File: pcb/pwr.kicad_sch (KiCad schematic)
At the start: 17 parts, among them IC1 LT8606IDC#TRPBF

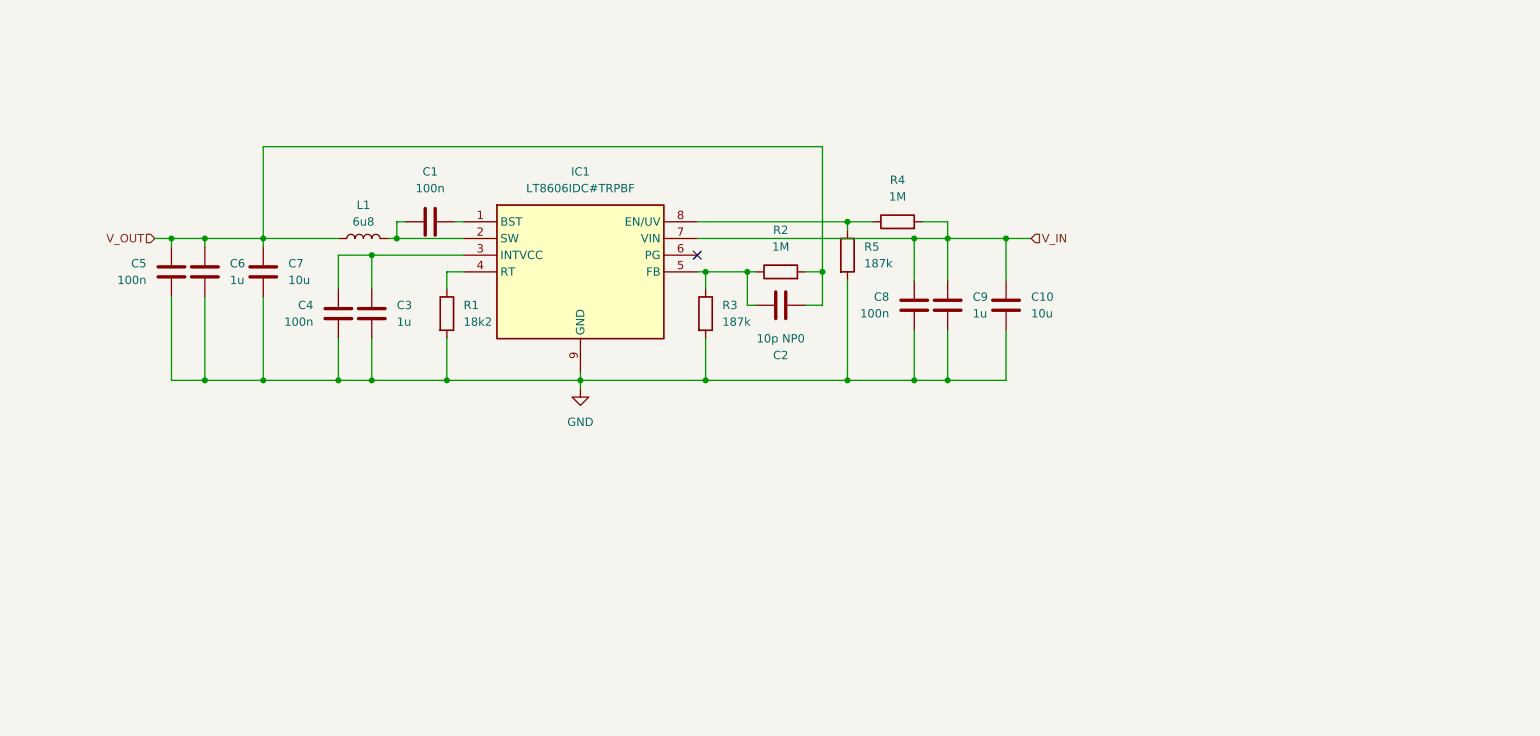
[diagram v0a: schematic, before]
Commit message: Sch almost done, maybe add current sense
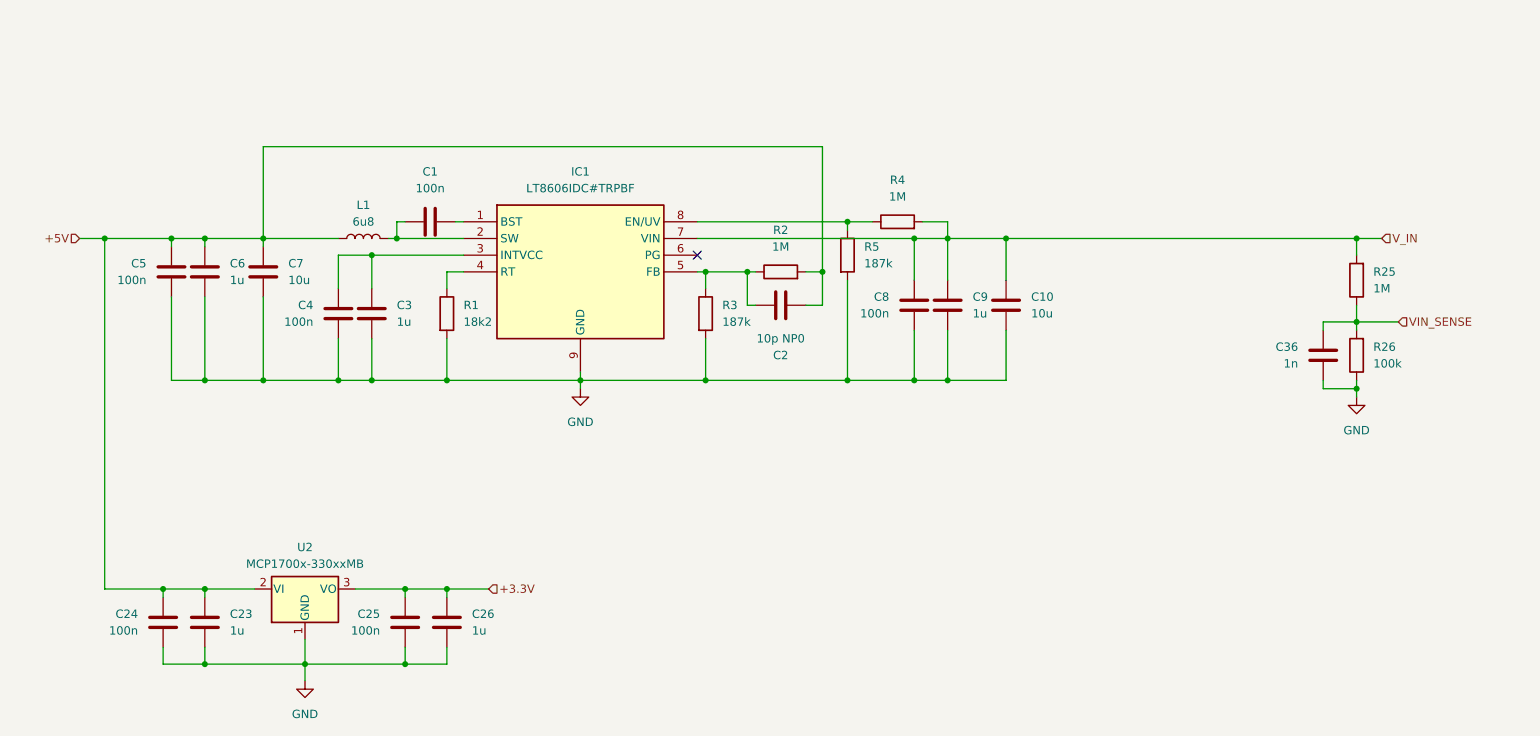
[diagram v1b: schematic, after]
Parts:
- added C23, C26: 1u, Capacitor_SMD:C_0603_1608Metric, symbol Device:C
- added C24, C25: 100n, Capacitor_SMD:C_0603_1608Metric, symbol Device:C
- added C36: 1n, Capacitor_SMD:C_0603_1608Metric, symbol Device:C
- added R25: 1M, Resistor_SMD:R_0603_1608Metric, symbol Device:R
- added R26: 100k, Resistor_SMD:R_0603_1608Metric, symbol Device:R
- added U2: MCP1700x-330xxMB, Package_TO_SOT_SMD:SOT-89-3, symbol Regulator_Linear:MCP1700x-330xxMB
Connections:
- net GND: now also C23.2, C24.1, C25.1, C26.2, C36.1, R26.1, U2.1 (GND)
- net V_IN: now also R25.2
- net V_OUT renamed +5V
- net +5V: now also C23.1, C24.2, U2.2 (VI)
- new net +3.3V: C25.2, C26.1, U2.3 (VO)
- new net VIN_SENSE: C36.2, R25.1, R26.2

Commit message: Scheamtic almost finished, astarted firmware and pcb
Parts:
- added C37: 100n, Capacitor_SMD:C_0603_1608Metric, symbol Device:C
- added D10: BAV199, Package_TO_SOT_SMD:TSOT-23, symbol Device:D_Dual_Series_AKC
- added R27: 500m, Resistor_SMD:R_0603_1608Metric, symbol Device:R
- added U3: INA186A4IDCKR, INA186A4IDCKR:SOT65P210X110-6N, symbol INA186A4IDCKR:INA186A4IDCKR
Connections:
- net +3.3V: now also D10.2 (K)
- net GND: now also C37.1, D10.1 (A), U3.1, U3.2
- net VIN_SENSE: now also D10.3 (common)
- net V_IN: now also R27.1, U3.4; no longer C10.1, C8.2, C9.1, IC1.7 (VIN), R4.2
- new net: C10.1, C8.2, C9.1, IC1.7 (VIN), R27.2, R4.2, U3.5
- new net EN_I_SENS: C37.2, U3.3
- new net I_SENS: U3.6
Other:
- moved on the sheet: C1, C10, C2, C23, C24, C25, C26, C3, C36, C4, C5, C6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

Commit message: Schematic finished, first routing
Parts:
- added C44: 1n, Capacitor_SMD:C_0603_1608Metric, symbol Device:C
- added R28: 1k, Resistor_SMD:R_0603_1608Metric, symbol Device:R
- U3: footprint INA186A4IDCKR:SOT65P210X110-6N -> lib_local:SOT65P210X110-6N
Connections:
- net GND: now also C44.1
- net I_SENS: now also C44.2, R28.1; no longer U3.6
- new net: R28.2, U3.6
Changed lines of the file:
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@@
 	)
 	(junction
+		(at 193.04 128.27)
+		(diameter 0)
+		(color 0 0 0 0)
+	)
+	(junction
 		(at 250.19 86.36)
 		(diameter 0)
@@
 	)
 	(junction
+		(at 170.18 118.11)
+		(diameter 0)
+		(color 0 0 0 0)
+	)
+	(junction
 		(at 166.37 64.77)
 		(diameter 0)
@@
 	)
 	(junction
-		(at 193.04 128.27)
+		(at 224.79 59.69)
 		(diameter 0)
 		(color 0 0 0 0)
 	)
 	(junction
-		(at 224.79 59.69)
+		(at 101.6 59.69)
 		(diameter 0)
 		(color 0 0 0 0)
 	)
 	(junction
-		(at 101.6 59.69)
+		(at 186.69 128.27)
 		(diameter 0)
 		(color 0 0 0 0)
@@
 	(wire
 		(pts
+			(xy 170.18 118.11) (xy 172.72 118.11)
+		)
+		(stroke
+			(width 0)
+			(type default)
+		)
+	)
+	(wire
+		(pts
 			(xy 66.04 113.03) (xy 72.39 113.03)
 		)
@@
 	(wire
 		(pts
+			(xy 180.34 118.11) (xy 182.88 118.11)
+		)
+		(stroke
+			(width 0)
+			(type default)
+		)
+	)
+	(wire
+		(pts
 			(xy 180.34 59.69) (xy 185.42 59.69)
 		)
@@
 	(wire
 		(pts
-			(xy 193.04 128.27) (xy 193.04 130.81)
+			(xy 170.18 128.27) (xy 186.69 128.27)
+		)
+		(stroke
+			(width 0)
+			(type default)
+		)
+	)
+	(wire
+		(pts
+			(xy 193.04 128.27) (xy 193.04 134.62)
 		)
 		(stroke
@@
 	(wire
 		(pts
+			(xy 170.18 118.11) (xy 170.18 119.38)
+		)
+		(stroke
+			(width 0)
+			(type default)
+		)
+	)
+	(wire
+		(pts
 			(xy 185.42 59.69) (xy 194.31 59.69)
 		)
@@
 	(wire
 		(pts
-			(xy 176.53 118.11) (xy 182.88 118.11)
+			(xy 165.1 118.11) (xy 170.18 118.11)
 		)
 		(stroke
@@
 	(wire
 		(pts
+			(xy 170.18 127) (xy 170.18 128.27)
+		)
+		(stroke
+			(width 0)
+			(type default)
+		)
+	)
+	(wire
+		(pts
 			(xy 241.3 95.25) (xy 241.3 96.52)
 		)
@@
 	(hierarchical_label "I_SENS"
 		(shape output)
-		(at 176.53 118.11 180)
+		(at 165.1 118.11 180)
 		(effects
 			(font
@@
 	)
 	(symbol
+		(lib_id "Device:R")
+		(at 176.53 118.11 90)
+		(mirror x)
+		(unit 1)
+		(body_style 1)
+		(exclude_from_sim no)
+		(in_bom yes)
+		(on_board yes)
+		(in_pos_files yes)
+		(dnp no)
+		(property "Reference" "R28"
+			(at 176.53 124.46 90)
+			(show_name no)
+			(do_not_autoplace no)
+			(effects
+				(font
+					(size 1.27 1.27)
+				)
+			)
+		)
+		(property "Value" "1k"
+			(at 176.53 121.92 90)
+			(show_name no)
+			(do_not_autoplace no)
+			(effects
+				(font
+					(size 1.27 1.27)
+				)
+			)
+		)
+		(property "Footprint" "Resistor_SMD:R_0603_1608Metric"
+			(at 176.53 116.332 90)
+			(hide yes)
+			(show_name no)
+			(do_not_autoplace no)
+			(effects
+				(font
+					(size 1.27 1.27)
+				)
+			)
+		)
+		(property "Datasheet" ""
+			(at 176.53 118.11 0)
+			(hide yes)
+			(show_name no)
+			(do_not_autoplace no)
+			(effects
+				(font
+					(size 1.27 1.27)
+				)
+			)
+		)
+		(property "Description" "Resistor"
+			(at 176.53 118.11 0)
+			(hide yes)
+			(show_name no)
+			(do_not_autoplace no)
+			(effects
+				(font
+					(size 1.27 1.27)
+				)
+			)
+		)
+		(pin "2"
+		)
+		(pin "1"
+		)
+		(instances
+			(project "geiger_probe"
+				(path "/eb6e66b6-2df0-4872-8f92-4c510b34f8fe/f2ffdc0d-50d8-4a85-929e-edddefffb681"
+					(reference "R28")
+					(unit 1)
+				)
+			)
+		)
+	)
+	(symbol
 		(lib_id "SamacSys_Parts:LT8606IDC#TRPBF")
 		(at 111.76 57.15 0)
@@
 	(symbol
 		(lib_id "power:GND")
-		(at 193.04 130.81 0)
+		(at 193.04 134.62 0)
 		(unit 1)
 		(body_style 1)
@@
 		(fields_autoplaced yes)
 		(property "Reference" "#PWR031"
-			(at 193.04 137.16 0)
+			(at 193.04 140.97 0)
 			(hide yes)
 			(show_name no)
@@
 		)
 		(property "Value" "GND"
-			(at 193.04 135.89 0)
+			(at 193.04 139.7 0)
 			(show_name no)
 			(do_not_autoplace no)
@@
 		)
 		(property "Footprint" ""
-			(at 193.04 130.81 0)
+			(at 193.04 134.62 0)
 			(hide yes)
 			(show_name no)
@@
 		)
 		(property "Datasheet" ""
-			(at 193.04 130.81 0)
+			(at 193.04 134.62 0)
 			(hide yes)
 			(show_name no)
@@
 		)
 		(property "Description" "Power symbol creates a global label with name \"GND\" , ground"
-			(at 193.04 130.81 0)
+			(at 193.04 134.62 0)
 			(hide yes)
 			(show_name no)
@@
 	(symbol
 		(lib_id "Device:C")
+		(at 170.18 123.19 0)
+		(mirror x)
+		(unit 1)
+		(body_style 1)
+		(exclude_from_sim no)
+		(in_bom yes)
+		(on_board yes)
+		(in_pos_files yes)
+		(dnp no)
+		(property "Reference" "C44"
+			(at 166.37 121.9199 0)
+			(show_name no)
+			(do_not_autoplace no)
+			(effects
+				(font
+					(size 1.27 1.27)
+				)
+				(justify right)
+			)
+		)
+		(property "Value" "1n"
+			(at 166.37 124.4599 0)
+			(show_name no)
+			(do_not_autoplace no)
+			(effects
+				(font
+					(size 1.27 1.27)
+				)
+				(justify right)
+			)
+		)
+		(property "Footprint" "Capacitor_SMD:C_0603_1608Metric"
+			(at 171.1452 119.38 0)
+			(hide yes)
+			(show_name no)
+			(do_not_autoplace no)
+			(effects
+				(font
+					(size 1.27 1.27)
+				)
+			)
+		)
+		(property "Datasheet" ""
+			(at 170.18 123.19 0)
+			(hide yes)
+			(show_name no)
+			(do_not_autoplace no)
+			(effects
+				(font
+					(size 1.27 1.27)
+				)
+			)
+		)
+		(property "Description" "Unpolarized capacitor"
+			(at 170.18 123.19 0)
+			(hide yes)
+			(show_name no)
+			(do_not_autoplace no)
+			(effects
+				(font
+					(size 1.27 1.27)
+				)
+			)
+		)
+		(pin "1"
+		)
+		(pin "2"
+		)
+		(instances
+			(project "geiger_probe"
+				(path "/eb6e66b6-2df0-4872-8f92-4c510b34f8fe/f2ffdc0d-50d8-4a85-929e-edddefffb681"
+					(reference "C44")
+					(unit 1)
+				)
+			)
+		)
+	)
+	(symbol
+		(lib_id "Device:C")
 		(at 67.31 64.77 0)
 		(mirror x)
@@
 			)
 		)
-		(property "Footprint" "INA186A4IDCKR:SOT65P210X110-6N"
+		(property "Footprint" "lib_local:SOT65P210X110-6N"
 			(at 195.58 118.11 0)
 			(hide yes)

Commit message: Cleaning
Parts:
- C2: Manufacturer_Part_Number (none) -> 0603N100J500CT
- D10: Manufacturer_Part_Number (none) -> BAV199
- L1: Manufacturer_Part_Number (none) -> LQH32PN6R8NN0L
- R27: Manufacturer_Part_Number (none) -> CS0603-0R50-1%-HP
- U2: Manufacturer_Part_Number (none) -> MCP1700T-3302E/MB
- U3: Manufacturer_Part_Number (none) -> INA186A4IDCKR
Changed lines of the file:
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@@
+			)
+		)
+		(property "Manufacturer_Part_Number" "0603N100J500CT"
+			(at 160.02 69.85 90)
+			(hide yes)
+			(show_name no)
+			(do_not_autoplace no)
+			(effects
+				(font
+					(size 1.27 1.27)
+				)
 			)
 		)
@@
 			)
 		)
+		(property "Manufacturer_Part_Number" "CS0603-0R50-1%-HP"
+			(at 218.44 59.69 90)
+			(hide yes)
+			(show_name no)
+			(do_not_autoplace no)
+			(effects
+				(font
+					(size 1.27 1.27)
+				)
+			)
+		)
 		(pin "2"
 		)
@@
 			)
 		)
+		(property "Manufacturer_Part_Number" "MCP1700T-3302E/MB"
+			(at 87.63 113.03 0)
+			(hide yes)
+			(show_name no)
+			(do_not_autoplace no)
+			(effects
+				(font
+					(size 1.27 1.27)
+				)
+			)
+		)
 		(pin "2"
 		)
@@
 			)
 		)
+		(property "Manufacturer_Part_Number" "LQH32PN6R8NN0L"
+			(at 96.52 59.69 90)
+			(hide yes)
+			(show_name no)
+			(do_not_autoplace no)
+			(effects
+				(font
+					(size 1.27 1.27)
+				)
+			)
+		)
 		(pin "2"
 		)
@@
 			)
 		)
+		(property "Manufacturer_Part_Number" "BAV199"
+			(at 266.7 86.36 90)
+			(hide yes)
+			(show_name no)
+			(do_not_autoplace no)
+			(effects
+				(font
+					(size 1.27 1.27)
+				)
+			)
+		)
 		(pin "1"
 		)
@@
 			)
 		)
+		(property "Manufacturer_Part_Number" "INA186A4IDCKR"
+			(at 195.58 118.11 0)
+			(hide yes)
+			(show_name no)
+			(do_not_autoplace no)
+			(effects
+				(font
+					(size 1.27 1.27)
+				)
+			)
+		)

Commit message: Cleaning
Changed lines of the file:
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@@
 	)
 	(junction
+		(at 193.04 96.52)
+		(diameter 0)
+		(color 0 0 0 0)
+	)
+	(junction
 		(at 109.22 81.28)
 		(diameter 0)
@@
 	(wire
 		(pts
+			(xy 57.15 58.42) (xy 57.15 59.69)
+		)
+		(stroke
+			(width 0)
+			(type default)
+		)
+	)
+	(wire
+		(pts
 			(xy 87.63 120.65) (xy 87.63 124.46)
 		)
@@
 	(wire
 		(pts
+			(xy 193.04 93.98) (xy 193.04 96.52)
+		)
+		(stroke
+			(width 0)
+			(type default)
+		)
+	)
+	(wire
+		(pts
 			(xy 212.09 59.69) (xy 214.63 59.69)
 		)
@@
 	)
 	(symbol
+		(lib_id "power:PWR_FLAG")
+		(at 193.04 93.98 0)
+		(unit 1)
+		(body_style 1)
+		(exclude_from_sim no)
+		(in_bom yes)
+		(on_board yes)
+		(in_pos_files yes)
+		(dnp no)
+		(fields_autoplaced yes)
+		(property "Reference" "#FLG04"
+			(at 193.04 92.075 0)
+			(hide yes)
+			(show_name no)
+			(do_not_autoplace no)
+			(effects
+				(font
+					(size 1.27 1.27)
+				)
+			)
+		)
+		(property "Value" "PWR_FLAG"
+			(at 193.04 88.9 0)
+			(show_name no)
+			(do_not_autoplace no)
+			(effects
+				(font
+					(size 1.27 1.27)
+				)
+			)
+		)
+		(property "Footprint" ""
+			(at 193.04 93.98 0)
+			(hide yes)
+			(show_name no)
+			(do_not_autoplace no)
+			(effects
+				(font
+					(size 1.27 1.27)
+				)
+			)
+		)
+		(property "Datasheet" ""
+			(at 193.04 93.98 0)
+			(hide yes)
+			(show_name no)
+			(do_not_autoplace no)
+			(effects
+				(font
+					(size 1.27 1.27)
+				)
+			)
+		)
+		(property "Description" "Special symbol for telling ERC where power comes from"
+			(at 193.04 93.98 0)
+			(hide yes)
+			(show_name no)
+			(do_not_autoplace no)
+			(effects
+				(font
+					(size 1.27 1.27)
+				)
+			)
+		)
+		(pin "1"
+		)
+		(instances
+			(project "geiger_probe"
+				(path "/eb6e66b6-2df0-4872-8f92-4c510b34f8fe/f2ffdc0d-50d8-4a85-929e-edddefffb681"
+					(reference "#FLG04")
+					(unit 1)
+				)
+			)
+		)
+	)
+	(symbol
 		(lib_id "Device:C")
 		(at 72.39 118.11 0)
@@
 					(unit 1)
 				)
+			)
+		)
+	)
+	(symbol
+		(lib_id "power:PWR_FLAG")
+		(at 57.15 58.42 0)
+		(unit 1)
+		(body_style 1)
+		(exclude_from_sim no)
+		(in_bom yes)
+		(on_board yes)
+		(in_pos_files yes)
+		(dnp no)
+		(fields_autoplaced yes)
+		(property "Reference" "#FLG03"
+			(at 57.15 56.515 0)
+			(hide yes)
+			(show_name no)
+			(do_not_autoplace no)
+			(effects
+				(font
+					(size 1.27 1.27)
+				)
+			)
+		)
+		(property "Value" "PWR_FLAG"
+			(at 57.15 53.34 0)
+			(show_name no)
+			(do_not_autoplace no)
+			(effects
+				(font
+					(size 1.27 1.27)
+				)
+			)
+		)
+		(property "Footprint" ""
+			(at 57.15 58.42 0)
+			(hide yes)
+			(show_name no)
+			(do_not_autoplace no)
+			(effects
+				(font
+					(size 1.27 1.27)
+				)
+			)
+		)
+		(property "Datasheet" ""
+			(at 57.15 58.42 0)
+			(hide yes)
+			(show_name no)
+			(do_not_autoplace no)
+			(effects
+				(font
+					(size 1.27 1.27)
+				)
+			)
+		)
+		(property "Description" "Special symbol for telling ERC where power comes from"
+			(at 57.15 58.42 0)
+			(hide yes)
+			(show_name no)
+			(do_not_autoplace no)
+			(effects
+				(font
+					(size 1.27 1.27)
+				)
+			)
+		)
+		(pin "1"
+		)
+		(instances
+			(project "geiger_probe"
+				(path "/eb6e66b6-2df0-4872-8f92-4c510b34f8fe/f2ffdc0d-50d8-4a85-929e-edddefffb681"
+					(reference "#FLG03")
+					(unit 1)
+				)

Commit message: Fix BOM data: correct MPNs for C16/C19, HV resistor part numbers for R9/R10/R12
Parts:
- R2, R25, R4: Manufacturer_Part_Number (none) -> CRCW06031M00FKTABC
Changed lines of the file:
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@@
 			)
 		)
-		(property "Description" "0603N100J500CT"
+		(property "Description" "Unpolarized capacitor"
 			(at 160.02 69.85 0)
 			(hide yes)
@@
 			)
 		)
-		(property "Description" "Resistor"
+		(property "Description" "CRCW06031M00FKTABC"
+			(at 241.3 80.01 0)
+			(hide yes)
+			(show_name no)
+			(do_not_autoplace no)
+			(effects
+				(font
+					(size 1.27 1.27)
+				)
+			)
+		)
+		(property "Manufacturer_Part_Number" "CRCW06031M00FKTABC"
 			(at 241.3 80.01 0)
 			(hide yes)
@@
 			)
 		)
-		(property "Description" "Resistor"
+		(property "Description" "CRCW06031M00FKTABC"
 			(at 177.8 57.15 0)
+			(hide yes)
+			(show_name no)
+			(do_not_autoplace no)
+			(effects
+				(font
+					(size 1.27 1.27)
+				)
+			)
+		)
+		(property "Manufacturer_Part_Number" "CRCW06031M00FKTABC"
+			(at 177.8 57.15 90)
 			(hide yes)
 			(show_name no)
@@
 			)
 		)
-		(property "Description" "Resistor"
+		(property "Description" "CRCW06031M00FKTABC"
 			(at 160.02 64.77 0)
 			(hide yes)
 			(show_name no)
+			(do_not_autoplace no)
+			(effects
+				(font
+					(size 1.27 1.27)
+				)
+			)
+		)
+		(property "Manufacturer_Part_Number" "CRCW06031M00FKTABC"
+			(at 160.02 64.77 90)
+			(hide yes)
+			(show_name no)
